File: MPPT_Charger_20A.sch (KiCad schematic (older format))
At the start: 2 parts

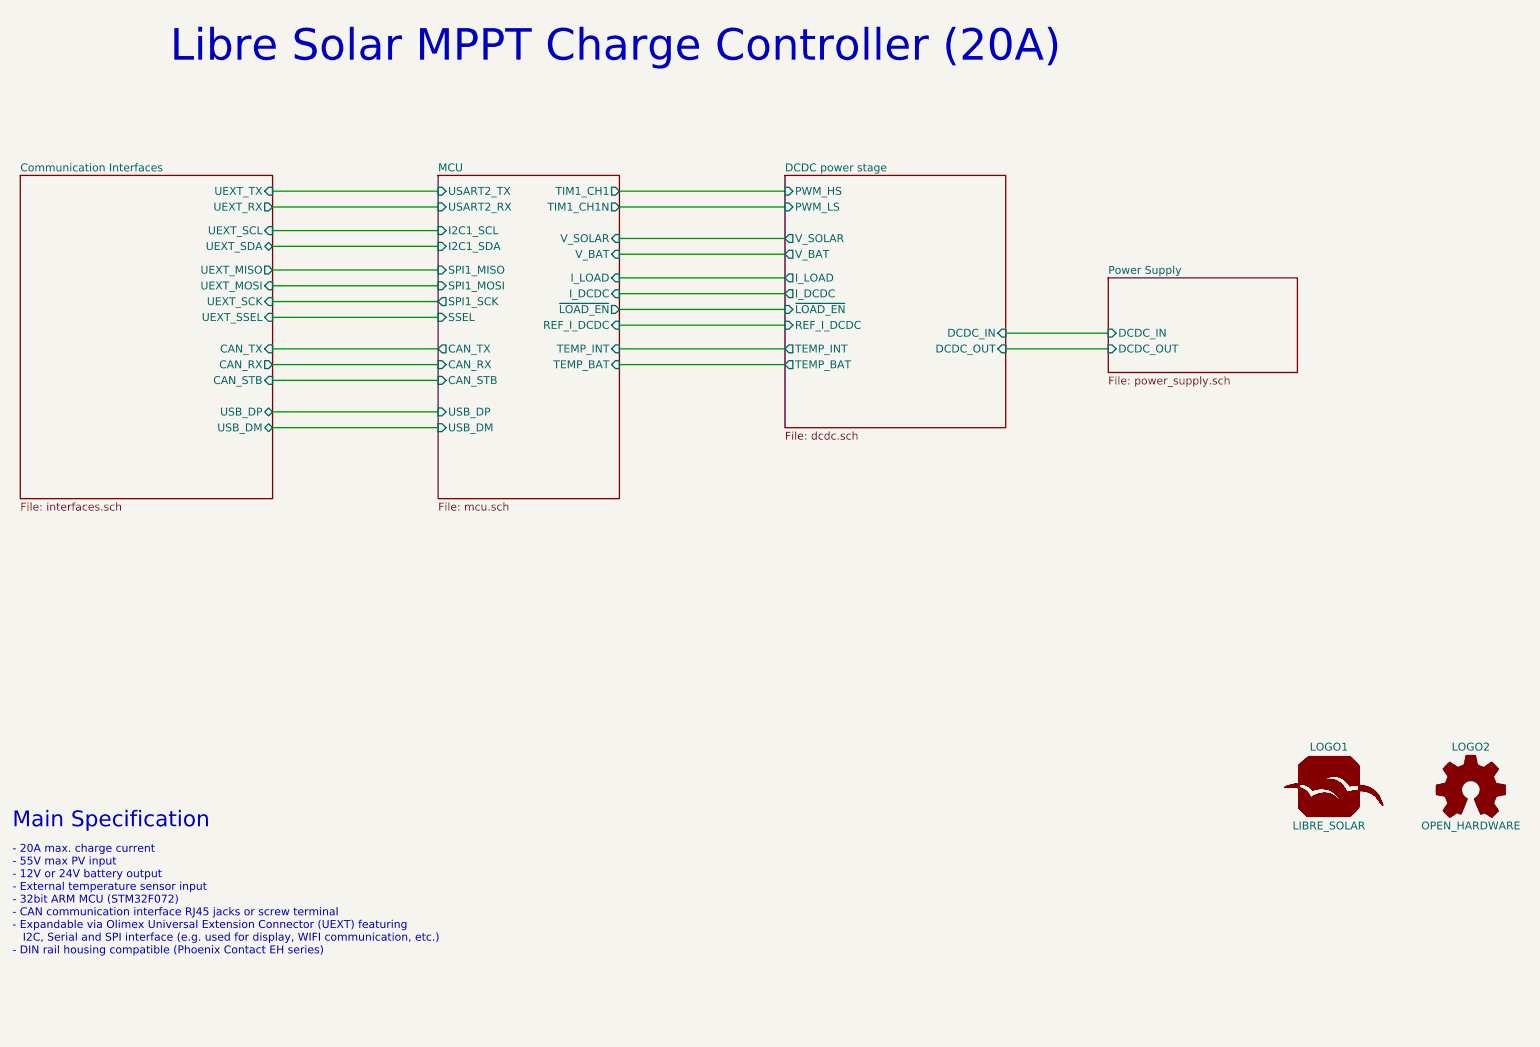
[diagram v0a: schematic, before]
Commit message: Updated R/C/L symbols to IEC 60617 style
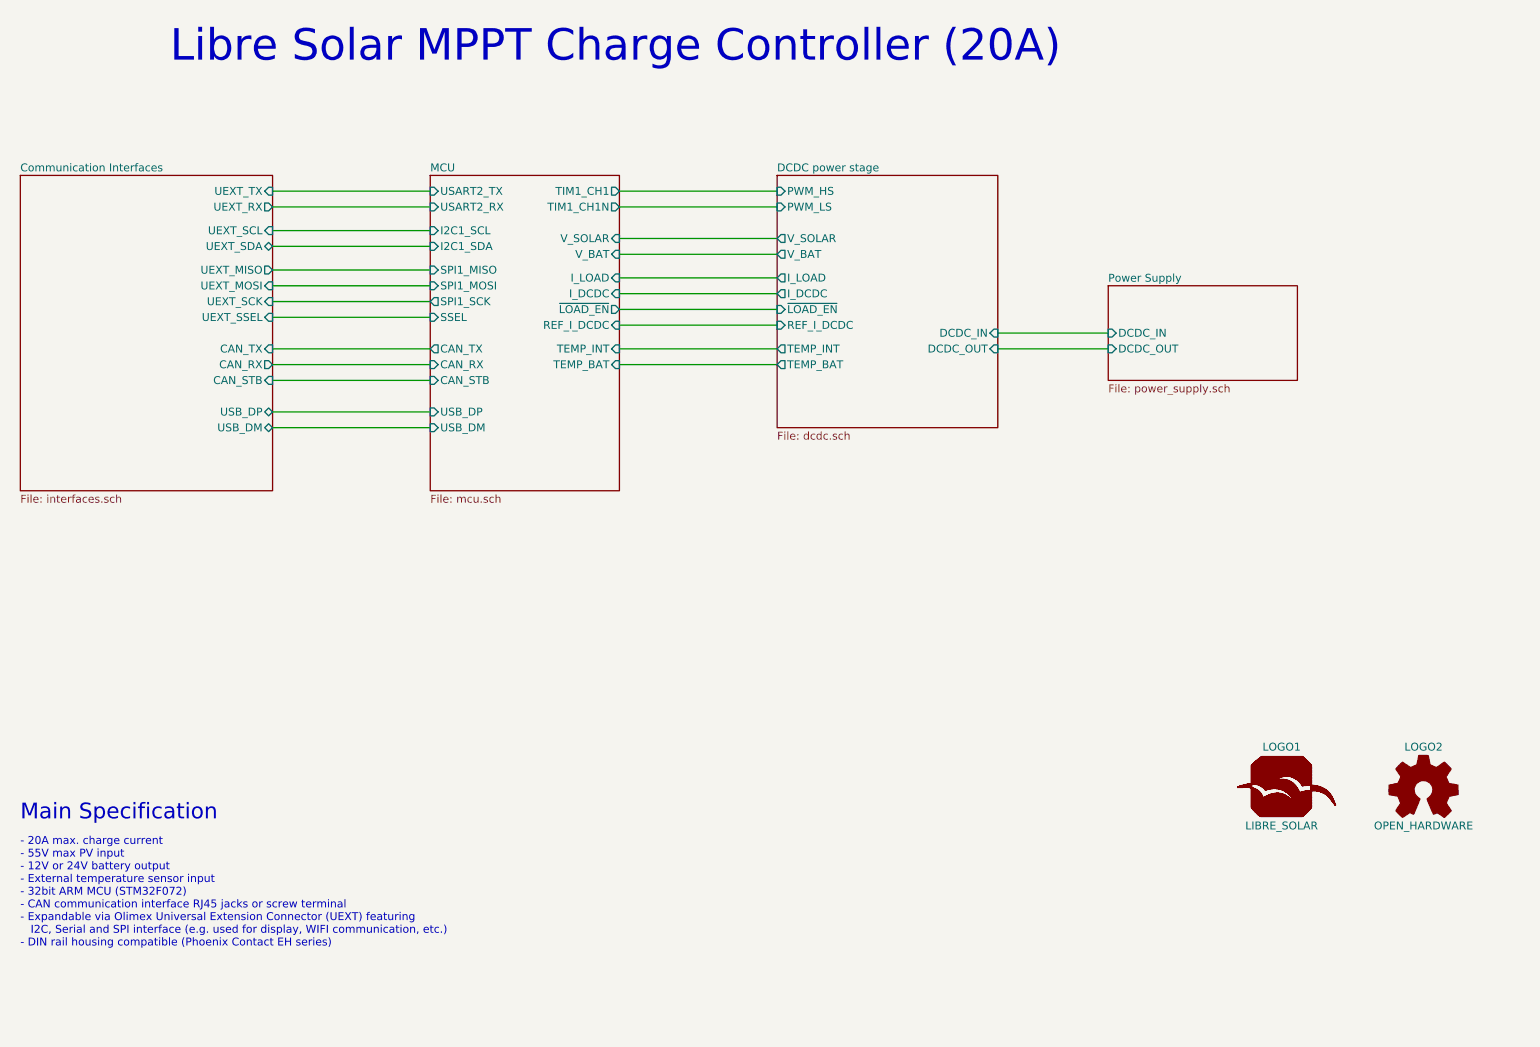
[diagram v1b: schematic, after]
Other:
- moved on the sheet: LOGO1, LOGO2
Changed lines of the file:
@@
 EESchema Schematic File Version 2
 LIBS:LibreSolar
+LIBS:IEC60617
 LIBS:device
 LIBS:power
@@
 LIBS:regul
 LIBS:dc-dc
+LIBS:74xgxx
+LIBS:74xx
+LIBS:ac-dc
+LIBS:actel
+LIBS:adc-dac
+LIBS:Altera
+LIBS:analog_devices
+LIBS:analog_switches
+LIBS:atmel
+LIBS:audio
+LIBS:battery_management
+LIBS:bbd
+LIBS:brooktre
+LIBS:cmos_ieee
+LIBS:cmos4000
+LIBS:contrib
+LIBS:cypress
+LIBS:digital-audio
+LIBS:diode
+LIBS:display
+LIBS:dsp
+LIBS:elec-unifil
+LIBS:ftdi
+LIBS:gennum
+LIBS:graphic
+LIBS:hc11
+LIBS:intel
+LIBS:interface
+LIBS:ir
+LIBS:Lattice
+LIBS:maxim
+LIBS:memory
+LIBS:microchip
+LIBS:microchip_dspic33dsc
+LIBS:microchip_pic10mcu
+LIBS:microchip_pic12mcu
+LIBS:microchip_pic16mcu
+LIBS:microchip_pic18mcu
+LIBS:microchip_pic32mcu
+LIBS:microcontrollers
+LIBS:motor_drivers
+LIBS:motorola
+LIBS:msp430
+LIBS:nordicsemi
+LIBS:nxp_armmcu
+LIBS:onsemi
+LIBS:opto
+LIBS:Oscillators
+LIBS:philips
+LIBS:Power_Management
+LIBS:powerint
+LIBS:pspice
+LIBS:references
+LIBS:relays
+LIBS:rfcom
+LIBS:sensors
+LIBS:silabs
+LIBS:siliconi
+LIBS:stm8
+LIBS:stm32
+LIBS:supertex
+LIBS:switches
+LIBS:texas
+LIBS:transf
+LIBS:ttl_ieee
+LIBS:valves
+LIBS:video
+LIBS:Worldsemi
+LIBS:Xicor
+LIBS:xilinx
+LIBS:Zilog
+LIBS:SymbolsSimilarEN60617_oldDIN617-RevC-en
 LIBS:MPPT_charger_20A-cache
 EELAYER 25 0
@@
 $EndDescr
 $Sheet
-S 6350 2100 1400 1600
+S 6300 2100 1400 1600
 U 58A68DC9
 F0 "DCDC power stage" 50
 F1 "dcdc.sch" 50
-F2 "PWM_HS" I L 6350 2200 50
-F3 "PWM_LS" I L 6350 2300 50
-F4 "V_SOLAR" O L 6350 2500 50
-F5 "V_BAT" O L 6350 2600 50
-F6 "I_LOAD" O L 6350 2750 50
-F7 "I_DCDC" O L 6350 2850 50
-F8 "~LOAD_EN" I L 6350 2950 50
-F9 "REF_I_DCDC" I L 6350 3050 50
-F10 "DCDC_OUT" I R 7750 3200 50
-F11 "DCDC_IN" I R 7750 3100 50
-F12 "TEMP_INT" O L 6350 3200 50
-F13 "TEMP_BAT" O L 6350 3300 50
-$EndSheet
-$Sheet
-S 4150 2100 1150 2050
+F2 "PWM_HS" I L 6300 2200 50
+F3 "PWM_LS" I L 6300 2300 50
+F4 "V_SOLAR" O L 6300 2500 50
+F5 "V_BAT" O L 6300 2600 50
+F6 "I_LOAD" O L 6300 2750 50
+F7 "I_DCDC" O L 6300 2850 50
+F8 "~LOAD_EN" I L 6300 2950 50
+F9 "REF_I_DCDC" I L 6300 3050 50
+F10 "DCDC_OUT" I R 7700 3200 50
+F11 "DCDC_IN" I R 7700 3100 50
+F12 "TEMP_INT" O L 6300 3200 50
+F13 "TEMP_BAT" O L 6300 3300 50
+$EndSheet
+$Sheet
+S 4100 2100 1200 2000
 U 58A68DCB
 F0 "MCU" 50
@@
 F7 "I_LOAD" I R 5300 2750 50
 F8 "I_DCDC" I R 5300 2850 50
-F9 "CAN_TX" O L 4150 3200 50
-F10 "CAN_RX" I L 4150 3300 50
-F11 "I2C1_SDA" I L 4150 2550 50
-F12 "I2C1_SCL" I L 4150 2450 50
-F13 "SPI1_MOSI" I L 4150 2800 50
-F14 "SPI1_MISO" I L 4150 2700 50
-F15 "SPI1_SCK" O L 4150 2900 50
-F16 "SSEL" I L 4150 3000 50
-F17 "USB_DM" I L 4150 3700 50
-F18 "USB_DP" I L 4150 3600 50
-F19 "CAN_STB" I L 4150 3400 50
+F9 "CAN_TX" O L 4100 3200 50
+F10 "CAN_RX" I L 4100 3300 50
+F11 "I2C1_SDA" I L 4100 2550 50
+F12 "I2C1_SCL" I L 4100 2450 50
+F13 "SPI1_MOSI" I L 4100 2800 50
+F14 "SPI1_MISO" I L 4100 2700 50
+F15 "SPI1_SCK" O L 4100 2900 50
+F16 "SSEL" I L 4100 3000 50
+F17 "USB_DM" I L 4100 3700 50
+F18 "USB_DP" I L 4100 3600 50
+F19 "CAN_STB" I L 4100 3400 50
 F20 "REF_I_DCDC" I R 5300 3050 50
-F21 "USART2_RX" I L 4150 2300 50
-F22 "USART2_TX" I L 4150 2200 50
+F21 "USART2_RX" I L 4100 2300 50
+F22 "USART2_TX" I L 4100 2200 50
 F23 "TEMP_INT" I R 5300 3200 50
 F24 "TEMP_BAT" I R 5300 3300 50
 $EndSheet
 $Sheet
-S 8400 2750 1200 600
+S 8400 2800 1200 600
 U 58C18D5C
 F0 "Power Supply" 50
@@
 $EndSheet
 Wire Wire Line
-	5300 2200 6350 2200
-Wire Wire Line
-	6350 2300 5300 2300
-Wire Wire Line
-	5300 2500 6350 2500
-Wire Wire Line
-	5300 2600 6350 2600
-Wire Wire Line
-	6350 2750 5300 2750
-Wire Wire Line
-	5300 2850 6350 2850
-Wire Wire Line
-	6350 2950 5300 2950
-$Sheet
-S 1500 2100 1600 2050
+	5300 2200 6300 2200
+Wire Wire Line
+	6300 2300 5300 2300
+Wire Wire Line
+	5300 2500 6300 2500
+Wire Wire Line
+	5300 2600 6300 2600
+Wire Wire Line
+	6300 2750 5300 2750
+Wire Wire Line
+	5300 2850 6300 2850
+Wire Wire Line
+	6300 2950 5300 2950
+$Sheet
+S 1500 2100 1600 2000
 U 58BE3089
 F0 "Communication Interfaces" 50
@@
 $EndSheet
 Wire Wire Line
-	3100 2200 4150 2200
-Wire Wire Line
-	4150 2300 3100 2300
-Wire Wire Line
-	3100 3000 4150 3000
-Wire Wire Line
-	4150 2900 3100 2900
-Wire Wire Line
-	3100 2800 4150 2800
-Wire Wire Line
-	4150 2700 3100 2700
-Wire Wire Line
-	3100 2550 4150 2550
-Wire Wire Line
-	4150 2450 3100 2450
-Wire Wire Line
-	3100 3200 4150 3200
-Wire Wire Line
-	4150 3300 3100 3300
-Wire Wire Line
-	3100 3400 4150 3400
-Wire Wire Line
-	4150 3600 3100 3600
-Wire Wire Line
-	3100 3700 4150 3700
-Wire Wire Line
-	5300 3050 6350 3050
-Wire Wire Line
-	5300 3200 6350 3200
+	3100 2200 4100 2200
+Wire Wire Line
+	4100 2300 3100 2300
+Wire Wire Line
+	3100 3000 4100 3000
+Wire Wire Line
+	4100 2900 3100 2900
+Wire Wire Line
+	3100 2800 4100 2800
+Wire Wire Line
+	4100 2700 3100 2700
+Wire Wire Line
+	3100 2550 4100 2550
+Wire Wire Line
+	4100 2450 3100 2450
+Wire Wire Line
+	3100 3200 4100 3200
+Wire Wire Line
+	4100 3300 3100 3300
+Wire Wire Line
+	3100 3400 4100 3400
+Wire Wire Line
+	4100 3600 3100 3600
+Wire Wire Line
+	3100 3700 4100 3700
+Wire Wire Line
+	5300 3050 6300 3050
+Wire Wire Line
+	5300 3200 6300 3200
 Text Notes 2450 1400 0    200  ~ 0
 Libre Solar MPPT Charge Controller (20A)
-Text Notes 1450 6250 0    100  ~ 0
+Text Notes 1500 6200 0    100  ~ 0
 Main Specification
-Text Notes 1450 7050 0    50   ~ 0
+Text Notes 1500 7000 0    50   ~ 0
 - 20A max. charge current\n- 55V max PV input\n- 12V or 24V battery output\n- External temperature sensor input\n- 32bit ARM MCU (STM32F072)\n- CAN communication interface RJ45 jacks or screw terminal\n- Expandable via Olimex Universal Extension Connector (UEXT) featuring\n   I2C, Serial and SPI interface (e.g. used for display, WIFI communication, etc.)\n- DIN rail housing compatible (Phoenix Contact EH series)\n
 $Comp
 L OPEN_HARDWARE_1 LOGO2
 U 1 1 58C36283
-P 10700 6000
-F 0 "LOGO2" H 10700 6275 50  0000 C CNN
-F 1 "OPEN_HARDWARE" H 10700 5775 50  0000 C CNN
-F 2 "Symbols:OSHW-Logo_5.7x6mm_SilkScreen" H 10700 6000 60  0001 C CNN
-F 3 "" H 10700 6000 60  0001 C CNN
-	1    10700 6000
+P 10400 6000
+F 0 "LOGO2" H 10400 6275 50  0000 C CNN
+F 1 "OPEN_HARDWARE" H 10400 5775 50  0000 C CNN
+F 2 "Symbols:OSHW-Logo_5.7x6mm_SilkScreen" H 10400 6000 60  0001 C CNN
+F 3 "" H 10400 6000 60  0001 C CNN
+	1    10400 6000
 	1    0    0    -1
 $EndComp
@@
 L LIBRE_SOLAR LOGO1
 U 1 1 58C39FC7
-P 9800 6000
-F 0 "LOGO1" H 9800 6275 50  0000 C CNN
-F 1 "LIBRE_SOLAR" H 9800 5775 50  0000 C CNN
-F 2 "LibreSolar:LIBRESOLAR_LOGO" H 9820 5990 60  0001 C CNN
-F 3 "" H 9820 5990 60  0001 C CNN
-	1    9800 6000
+P 9500 6000
+F 0 "LOGO1" H 9500 6275 50  0000 C CNN
+F 1 "LIBRE_SOLAR" H 9500 5775 50  0000 C CNN
+F 2 "LibreSolar:LIBRESOLAR_LOGO" H 9520 5990 60  0001 C CNN
+F 3 "" H 9520 5990 60  0001 C CNN
+	1    9500 6000
 	1    0    0    -1
 $EndComp
 Wire Wire Line
-	7750 3100 8400 3100
-Wire Wire Line
-	8400 3200 7750 3200
-Wire Wire Line
-	5300 3300 6350 3300
+	7700 3100 8400 3100
+Wire Wire Line
+	8400 3200 7700 3200
+Wire Wire Line
+	5300 3300 6300 3300
 $EndSCHEMATC

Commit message: Updated revision: 0.8
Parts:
- added J5: CONN_01X03, LibreSolar:Phoenix_Contact_MC_1,5_3-G-3,81, symbol CONN_01X03
- added MK1, MK2, MK3: Mounting_Hole, Mounting_Holes:MountingHole_3.2mm_M3, symbol Mounting_Hole
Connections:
- new net Analog Frontend/TEMP_BAT: J5.1 (P1)
- new net Communication Interfaces/5V_OUT: J5.3 (P3)
- new net GND: J5.2 (P2)
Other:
- note added: "Analog"
- note added: "DC/DC"
- note added: "Power"
- note added: "UEXT\nCAN\nUSB"
- note added: "µC"

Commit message: V0.8.1: Small changes and update to new kicad symbol library table (nightlies only)
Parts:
- J5: symbol CONN_01X03 -> Connector:Conn_01x03
- LOGO1: symbol LIBRE_SOLAR -> LibreSolar:LIBRE_SOLAR
- LOGO2: symbol OPEN_HARDWARE_1 -> Graphic:Logo_Open_Hardware_Small
- MK1, MK2, MK3: symbol Mounting_Hole -> Mechanical:Mounting_Hole
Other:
- moved on the sheet: LOGO1, LOGO2, MK1, MK2, MK3
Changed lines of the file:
@@
-EESchema Schematic File Version 2
-LIBS:MPPT_charger_20A-rescue
-LIBS:LibreSolar
-LIBS:IEC-60617
-LIBS:power
-LIBS:device
-LIBS:regul
-LIBS:switches
-LIBS:conn
-LIBS:logo
-LIBS:mechanical
+EESchema Schematic File Version 4
 LIBS:MPPT_charger_20A-cache
 EELAYER 26 0
@@
 - 20A max. charge current\n- 55V max PV input\n- 12V or 24V battery output\n- External temperature sensor input\n- 32bit ARM MCU (STM32F072)\n- CAN communication interface RJ45 jacks or screw terminal\n- Expandable via Olimex Universal Extension Connector (UEXT) featuring\n   I2C, Serial and SPI interface (e.g. used for display, WIFI communication, etc.)\n- DIN rail housing compatible (Phoenix Contact EH series)\n
 $Comp
-L OPEN_HARDWARE_1 LOGO2
+L Graphic:Logo_Open_Hardware_Small LOGO2
 U 1 1 58C36283
-P 10400 6000
-F 0 "LOGO2" H 10400 6275 50  0000 C CNN
-F 1 "OPEN_HARDWARE" H 10400 5775 50  0000 C CNN
-F 2 "Symbols:OSHW-Logo_5.7x6mm_SilkScreen" H 10400 6000 60  0001 C CNN
-F 3 "" H 10400 6000 60  0001 C CNN
-	1    10400 6000
-	1    0    0    -1
-$EndComp
-$Comp
-L LIBRE_SOLAR LOGO1
+P 10550 6100
+F 0 "LOGO2" H 10550 6375 50  0000 C CNN
+F 1 "OPEN_HARDWARE" H 10550 5875 50  0000 C CNN
+F 2 "Symbols:OSHW-Logo_5.7x6mm_SilkScreen" H 10550 6100 60  0001 C CNN
+F 3 "" H 10550 6100 60  0001 C CNN
+	1    10550 6100
+	1    0    0    -1
+$EndComp
+$Comp
+L LibreSolar:LIBRE_SOLAR LOGO1
 U 1 1 58C39FC7
-P 9500 6000
-F 0 "LOGO1" H 9500 6275 50  0000 C CNN
-F 1 "LIBRE_SOLAR" H 9500 5775 50  0000 C CNN
-F 2 "LibreSolar:LIBRESOLAR_LOGO" H 9520 5990 60  0001 C CNN
-F 3 "" H 9520 5990 60  0001 C CNN
-	1    9500 6000
+P 9650 6100
+F 0 "LOGO1" H 9650 6375 50  0000 C CNN
+F 1 "LIBRE_SOLAR" H 9650 5875 50  0000 C CNN
+F 2 "LibreSolar:LIBRESOLAR_LOGO" H 9670 6090 60  0001 C CNN
+F 3 "" H 9670 6090 60  0001 C CNN
+	1    9650 6100
 	1    0    0    -1
 $EndComp
@@
 Connection ~ 8200 2500
 $Comp
-L Mounting_Hole MK1
+L Mechanical:Mounting_Hole MK1
 U 1 1 595388B0
-P 5900 6400
-F 0 "MK1" H 6000 6446 50  0000 L CNN
-F 1 "Mounting_Hole" H 6000 6355 50  0000 L CNN
-F 2 "Mounting_Holes:MountingHole_3.2mm_M3" H 5900 6400 50  0001 C CNN
-F 3 "" H 5900 6400 50  0001 C CNN
-	1    5900 6400
-	1    0    0    -1
-$EndComp
-$Comp
-L Mounting_Hole MK2
+P 6050 7050
+F 0 "MK1" H 6150 7096 50  0000 L CNN
+F 1 "Mounting_Hole" H 6150 7005 50  0000 L CNN
+F 2 "Mounting_Holes:MountingHole_3.2mm_M3" H 6050 7050 50  0001 C CNN
+F 3 "" H 6050 7050 50  0001 C CNN
+	1    6050 7050
+	1    0    0    -1
+$EndComp
+$Comp
+L Mechanical:Mounting_Hole MK2
 U 1 1 59538A86
-P 5900 6600
-F 0 "MK2" H 6000 6646 50  0000 L CNN
-F 1 "Mounting_Hole" H 6000 6555 50  0000 L CNN
-F 2 "Mounting_Holes:MountingHole_3.2mm_M3" H 5900 6600 50  0001 C CNN
-F 3 "" H 5900 6600 50  0001 C CNN
-	1    5900 6600
-	1    0    0    -1
-$EndComp
-$Comp
-L Mounting_Hole MK3
+P 6050 7250
+F 0 "MK2" H 6150 7296 50  0000 L CNN
+F 1 "Mounting_Hole" H 6150 7205 50  0000 L CNN
+F 2 "Mounting_Holes:MountingHole_3.2mm_M3" H 6050 7250 50  0001 C CNN
+F 3 "" H 6050 7250 50  0001 C CNN
+	1    6050 7250
+	1    0    0    -1
+$EndComp
+$Comp
+L Mechanical:Mounting_Hole MK3
 U 1 1 59538C18
-P 5900 6800
-F 0 "MK3" H 6000 6846 50  0000 L CNN
-F 1 "Mounting_Hole" H 6000 6755 50  0000 L CNN
-F 2 "Mounting_Holes:MountingHole_3.2mm_M3" H 5900 6800 50  0001 C CNN
-F 3 "" H 5900 6800 50  0001 C CNN
-	1    5900 6800
-	1    0    0    -1
-$EndComp
-$Comp
-L CONN_01X03 J5
+P 6050 7450
+F 0 "MK3" H 6150 7496 50  0000 L CNN
+F 1 "Mounting_Hole" H 6150 7405 50  0000 L CNN
+F 2 "Mounting_Holes:MountingHole_3.2mm_M3" H 6050 7450 50  0001 C CNN
+F 3 "" H 6050 7450 50  0001 C CNN
+	1    6050 7450
+	1    0    0    -1
+$EndComp
+$Comp
+L Connector:Conn_01x03 J5
 U 1 1 59553D8B
 P 2800 5200
@@
 $EndComp
 $Comp
-L GND #PWR01
+L power:GND #PWR01
 U 1 1 59553D94
 P 3500 5300
